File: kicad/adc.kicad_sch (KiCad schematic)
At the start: 7 parts, among them U1 ADS8691IPWR

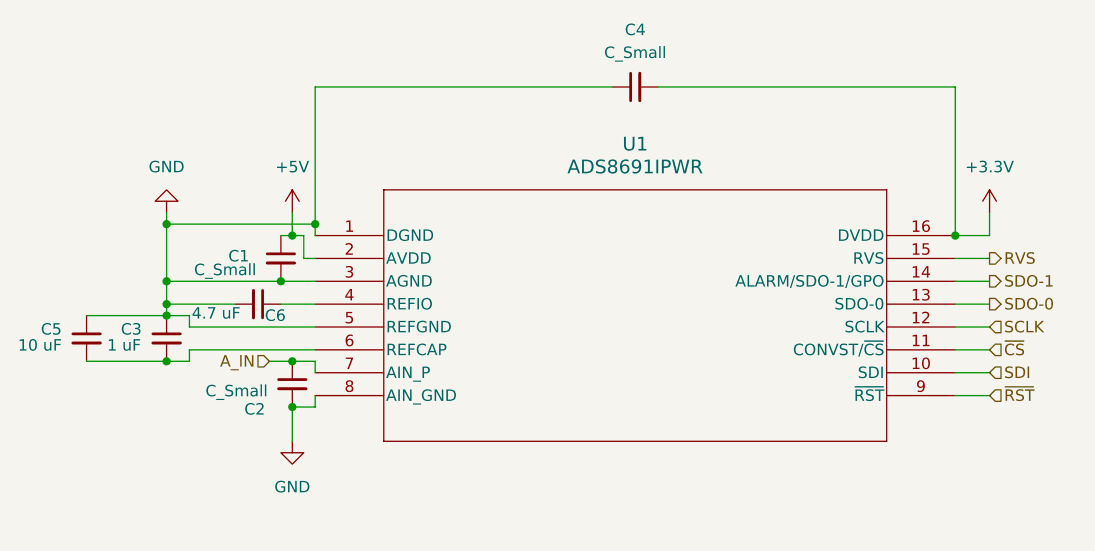
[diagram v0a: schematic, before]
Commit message: finish schematic for amp, and start routing (schematic isn't actually fully connected yet tho...)
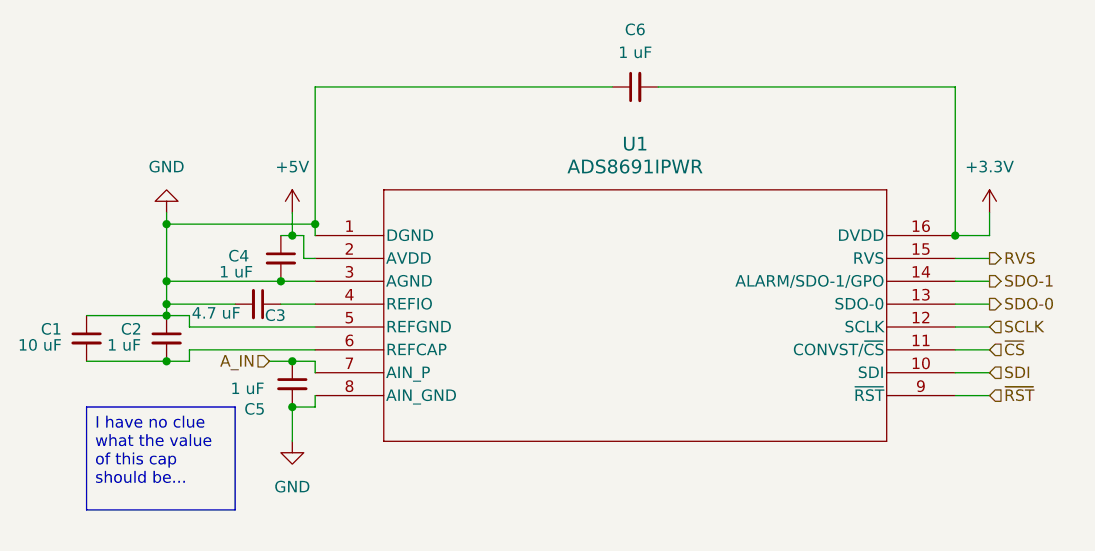
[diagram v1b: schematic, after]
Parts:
- C1: renamed from C5; footprint (none) -> Capacitor_SMD:C_0805_2012Metric
- C2: renamed from C3; footprint (none) -> Capacitor_SMD:C_0603_1608Metric
- C3: renamed from C6; footprint (none) -> Capacitor_SMD:C_0603_1608Metric
- C4: renamed from C1; value C_Small -> 1 uF; footprint (none) -> Capacitor_SMD:C_0603_1608Metric
- C5: renamed from C2; value C_Small -> 1 uF; footprint (none) -> Capacitor_SMD:C_0603_1608Metric
- C6: renamed from C4; value C_Small -> 1 uF; footprint (none) -> Capacitor_SMD:C_0603_1608Metric
- U1: footprint PW16_TEX -> strain-gauge:PW16_TEX
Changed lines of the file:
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@@
 	(generator_version "9.0")
 	(paper "A4")
+	(text_box "I have no clue what the value of this cap should be..."
+		(exclude_from_sim no)
+		(at 87.63 95.25 0)
+		(size 16.51 11.43)
+		(margins 0.9525 0.9525 0.9525 0.9525)
+		(stroke
+			(width 0)
+			(type solid)
+		)
+		(fill
+			(type none)
+		)
+		(effects
+			(font
+				(size 1.27 1.27)
+			)
+			(justify left top)
+		)
+	)
 	(junction
 		(at 96.52 83.82)
@@
 		(on_board yes)
 		(dnp no)
-		(property "Reference" "C6"
+		(property "Reference" "C3"
 			(at 107.442 85.09 90)
 			(effects
@@
 			)
 		)
-		(property "Footprint" ""
+		(property "Footprint" "Capacitor_SMD:C_0603_1608Metric"
 			(at 106.68 83.82 0)
 			(effects
@@
 			(project "strain-gauge"
 				(path "/cbc99ef0-5fa7-4678-bd4c-c2c08fe588b6/a931b1b9-f428-459e-895b-593f25a56a4b"
-					(reference "C6")
+					(reference "C3")
 					(unit 1)
 				)
@@
 		(dnp no)
 		(fields_autoplaced yes)
-		(property "Reference" "#PWR01"
+		(property "Reference" "#PWR06"
 			(at 110.49 105.41 0)
 			(effects
@@
 			(project ""
 				(path "/cbc99ef0-5fa7-4678-bd4c-c2c08fe588b6/a931b1b9-f428-459e-895b-593f25a56a4b"
-					(reference "#PWR01")
+					(reference "#PWR06")
 					(unit 1)
 				)
@@
 		(on_board yes)
 		(dnp no)
-		(property "Reference" "C2"
+		(property "Reference" "C5"
 			(at 105.156 95.504 0)
 			(effects
@@
 			)
 		)
-		(property "Value" "C_Small"
-			(at 100.838 93.472 0)
+		(property "Value" "1 uF"
+			(at 103.632 93.218 0)
 			(effects
 				(font
@@
 			)
 		)
-		(property "Footprint" ""
+		(property "Footprint" "Capacitor_SMD:C_0603_1608Metric"
 			(at 110.49 92.71 0)
 			(effects
@@
 			(project ""
 				(path "/cbc99ef0-5fa7-4678-bd4c-c2c08fe588b6/a931b1b9-f428-459e-895b-593f25a56a4b"
-					(reference "C2")
+					(reference "C5")
 					(unit 1)
 				)
@@
 		(dnp no)
 		(fields_autoplaced yes)
-		(property "Reference" "C4"
+		(property "Reference" "C6"
 			(at 148.5963 53.34 90)
 			(effects
@@
 			)
 		)
-		(property "Value" "C_Small"
+		(property "Value" "1 uF"
 			(at 148.5963 55.88 90)
 			(effects
@@
 			)
 		)
-		(property "Footprint" ""
+		(property "Footprint" "Capacitor_SMD:C_0603_1608Metric"
 			(at 148.59 59.69 0)
 			(effects
@@
 			(project ""
 				(path "/cbc99ef0-5fa7-4678-bd4c-c2c08fe588b6/a931b1b9-f428-459e-895b-593f25a56a4b"
-					(reference "C4")
+					(reference "C6")
 					(unit 1)
 				)
@@
 		(on_board yes)
 		(dnp no)
-		(property "Reference" "C1"
+		(property "Reference" "C4"
 			(at 103.378 78.486 0)
 			(effects
@@
 			)
 		)
-		(property "Value" "C_Small"
-			(at 99.568 80.01 0)
+		(property "Value" "1 uF"
+			(at 102.362 80.264 0)
 			(effects
 				(font
@@
 			)
 		)
-		(property "Footprint" ""
+		(property "Footprint" "Capacitor_SMD:C_0603_1608Metric"
 			(at 109.22 78.74 0)
 			(effects
@@
 			(project ""
 				(path "/cbc99ef0-5fa7-4678-bd4c-c2c08fe588b6/a931b1b9-f428-459e-895b-593f25a56a4b"
-					(reference "C1")
+					(reference "C4")
 					(unit 1)
 				)
@@
 		(dnp no)
 		(fields_autoplaced yes)
-		(property "Reference" "#PWR04"
+		(property "Reference" "#PWR07"
 			(at 187.96 77.47 0)
 			(effects
@@
 			(project ""
 				(path "/cbc99ef0-5fa7-4678-bd4c-c2c08fe588b6/a931b1b9-f428-459e-895b-593f25a56a4b"
-					(reference "#PWR04")
+					(reference "#PWR07")
 					(unit 1)
 				)
@@
 			)
 		)
-		(property "Footprint" "PW16_TEX"
+		(property "Footprint" "strain-gauge:PW16_TEX"
 			(at 113.03 76.2 0)
 			(effects
@@
 		(on_board yes)
 		(dnp no)
-		(property "Reference" "C5"
+		(property "Reference" "C1"
 			(at 82.55 86.614 0)
 			(effects
@@
 			)
 		)
-		(property "Footprint" ""
+		(property "Footprint" "Capacitor_SMD:C_0805_2012Metric"
 			(at 87.63 87.63 0)
 			(effects
@@
 			(project "strain-gauge"
 				(path "/cbc99ef0-5fa7-4678-bd4c-c2c08fe588b6/a931b1b9-f428-459e-895b-593f25a56a4b"
-					(reference "C5")
+					(reference "C1")
 					(unit 1)
 				)
@@
 		(dnp no)
 		(fields_autoplaced yes)
-		(property "Reference" "#PWR03"
+		(property "Reference" "#PWR05"
 			(at 110.49 77.47 0)
 			(effects
@@
 			(project ""
 				(path "/cbc99ef0-5fa7-4678-bd4c-c2c08fe588b6/a931b1b9-f428-459e-895b-593f25a56a4b"
-					(reference "#PWR03")
+					(reference "#PWR05")
 					(unit 1)
 				)
@@
 		(on_board yes)
 		(dnp no)
-		(property "Reference" "C3"
+		(property "Reference" "C2"
 			(at 91.44 86.614 0)
 			(effects
@@
 			)
 		)
-		(property "Footprint" ""
+		(property "Footprint" "Capacitor_SMD:C_0603_1608Metric"
 			(at 96.52 87.63 0)
 			(effects
@@
 			(project ""
 				(path "/cbc99ef0-5fa7-4678-bd4c-c2c08fe588b6/a931b1b9-f428-459e-895b-593f25a56a4b"
-					(reference "C3")
+					(reference "C2")
 					(unit 1)
 				)
@@
 		(dnp no)
 		(fields_autoplaced yes)
-		(property "Reference" "#PWR02"
+		(property "Reference" "#PWR04"
 			(at 96.52 67.31 0)
 			(effects
@@
 			(project ""
 				(path "/cbc99ef0-5fa7-4678-bd4c-c2c08fe588b6/a931b1b9-f428-459e-895b-593f25a56a4b"
-					(reference "#PWR02")
+					(reference "#PWR04")
 					(unit 1)
 				)

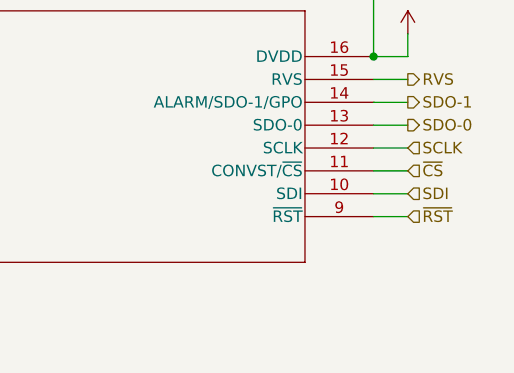
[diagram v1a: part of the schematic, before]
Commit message: started routing pcb
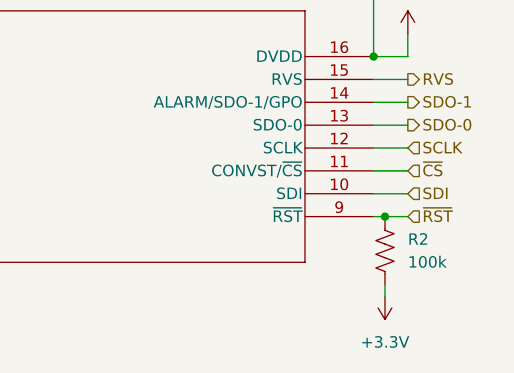
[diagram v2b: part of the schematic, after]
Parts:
- added R2: 100k, Resistor_SMD:R_0603_1608Metric, symbol Device:R_US
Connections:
- net +3.3V: now also R2.2
- net ~{RST}: now also R2.1
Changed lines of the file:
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@@
+	)
+	(junction
+		(at 185.42 93.98)
+		(diameter 0)
+		(color 0 0 0 0)
 	)
 	(junction
@@
 	(wire
 		(pts
-			(xy 184.15 93.98) (xy 187.96 93.98)
+			(xy 184.15 93.98) (xy 185.42 93.98)
 		)
 		(stroke
@@
 	(wire
 		(pts
+			(xy 185.42 101.6) (xy 185.42 102.87)
+		)
+		(stroke
+			(width 0)
+			(type default)
+		)
+	)
+	(wire
+		(pts
 			(xy 99.06 85.09) (xy 96.52 85.09)
 		)
@@
 		(pts
 			(xy 184.15 76.2) (xy 184.15 59.69)
+		)
+		(stroke
+			(width 0)
+			(type default)
+		)
+	)
+	(wire
+		(pts
+			(xy 185.42 93.98) (xy 187.96 93.98)
 		)
 		(stroke
@@
 	)
 	(symbol
+		(lib_id "Device:R_US")
+		(at 185.42 97.79 0)
+		(unit 1)
+		(exclude_from_sim no)
+		(in_bom yes)
+		(on_board yes)
+		(dnp no)
+		(fields_autoplaced yes)
+		(property "Reference" "R2"
+			(at 187.96 96.5199 0)
+			(effects
+				(font
+					(size 1.27 1.27)
+				)
+				(justify left)
+			)
+		)
+		(property "Value" "100k"
+			(at 187.96 99.0599 0)
+			(effects
+				(font
+					(size 1.27 1.27)
+				)
+				(justify left)
+			)
+		)
+		(property "Footprint" "Resistor_SMD:R_0603_1608Metric"
+			(at 186.436 98.044 90)
+			(effects
+				(font
+					(size 1.27 1.27)
+				)
+				(hide yes)
+			)
+		)
+		(property "Datasheet" "~"
+			(at 185.42 97.79 0)
+			(effects
+				(font
+					(size 1.27 1.27)
+				)
+				(hide yes)
+			)
+		)
+		(property "Description" "Resistor, US symbol"
+			(at 185.42 97.79 0)
+			(effects
+				(font
+					(size 1.27 1.27)
+				)
+				(hide yes)
+			)
+		)
+		(pin "1"
+		)
+		(pin "2"
+		)
+		(instances
+			(project ""
+				(path "/cbc99ef0-5fa7-4678-bd4c-c2c08fe588b6/a931b1b9-f428-459e-895b-593f25a56a4b"
+					(reference "R2")
+					(unit 1)
+				)
+			)
+		)
+	)
+	(symbol
 		(lib_id "Device:C_Small")
 		(at 148.59 59.69 90)
@@
 					(unit 1)
 				)
+			)
+		)
+	)
+	(symbol
+		(lib_id "power:+3.3V")
+		(at 185.42 102.87 180)
+		(unit 1)
+		(exclude_from_sim no)
+		(in_bom yes)
+		(on_board yes)
+		(dnp no)
+		(fields_autoplaced yes)
+		(property "Reference" "#PWR018"
+			(at 185.42 99.06 0)
+			(effects
+				(font
+					(size 1.27 1.27)
+				)
+				(hide yes)
+			)
+		)
+		(property "Value" "+3.3V"
+			(at 185.42 107.95 0)
+			(effects
+				(font
+					(size 1.27 1.27)
+				)
+			)
+		)
+		(property "Footprint" ""
+			(at 185.42 102.87 0)
+			(effects
+				(font
+					(size 1.27 1.27)
+				)
+				(hide yes)
+			)
+		)
+		(property "Datasheet" ""
+			(at 185.42 102.87 0)
+			(effects
+				(font
+					(size 1.27 1.27)
+				)
+				(hide yes)
+			)
+		)
+		(property "Description" "Power symbol creates a global label with name \"+3.3V\""
+			(at 185.42 102.87 0)
+			(effects
+				(font
+					(size 1.27 1.27)
+				)
+				(hide yes)
+			)
+		)
+		(pin "1"
+		)
+		(instances
+			(project ""
+				(path "/cbc99ef0-5fa7-4678-bd4c-c2c08fe588b6/a931b1b9-f428-459e-895b-593f25a56a4b"
+					(reference "#PWR018")
+					(unit 1)
+				)
